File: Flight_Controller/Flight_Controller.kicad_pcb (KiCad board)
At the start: 4 copper layers, 123 parts, among them IC1 ICM-20689, J1 USB_C_Receptacle_USB2.0_16P, J2 SM08B-SRSS-TB, J3 SM04B-SRSS-TB, J4 SM06B-SRSS-TBLFSN, J5 SM03B-SRSS-TB, Q1 AO3400A, SW1 SW_Push, U1 NO, U11 ESD224DQA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

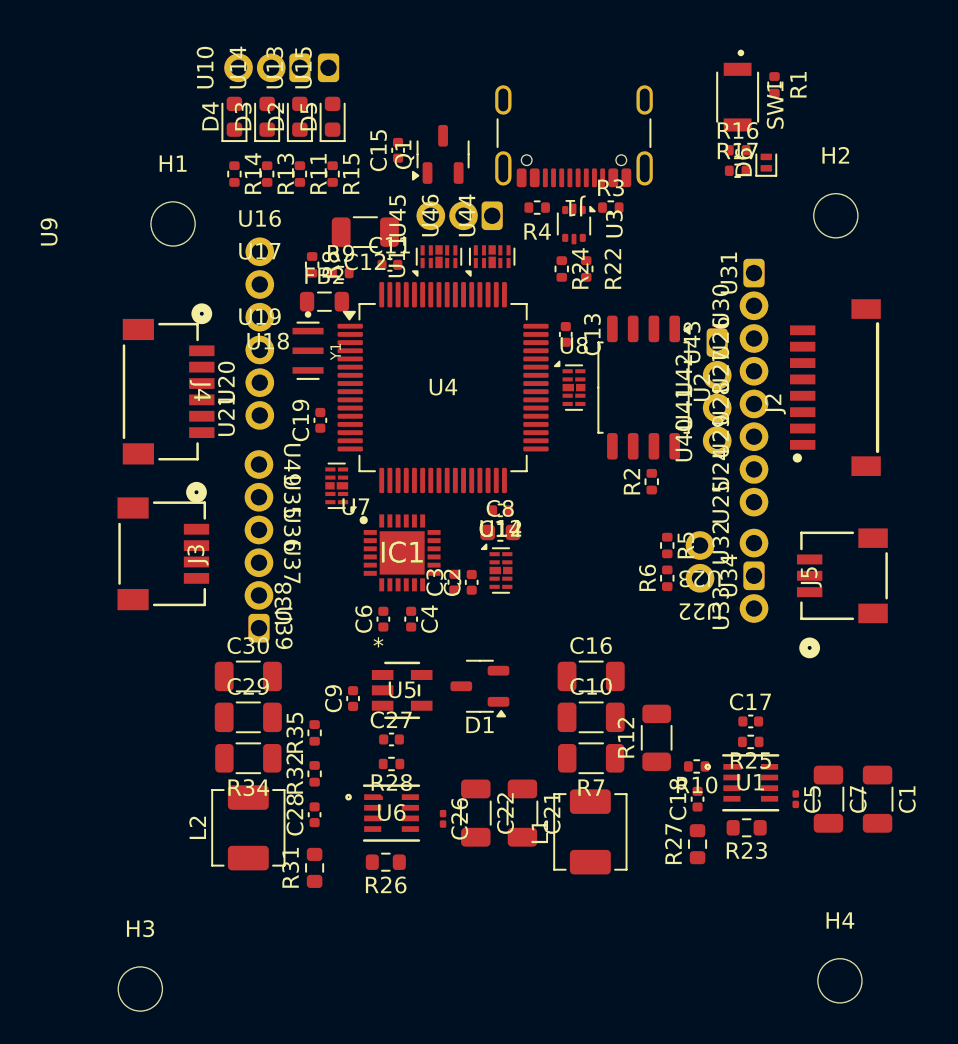
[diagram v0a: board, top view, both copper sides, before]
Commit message: Modificacion emplazamiento 2
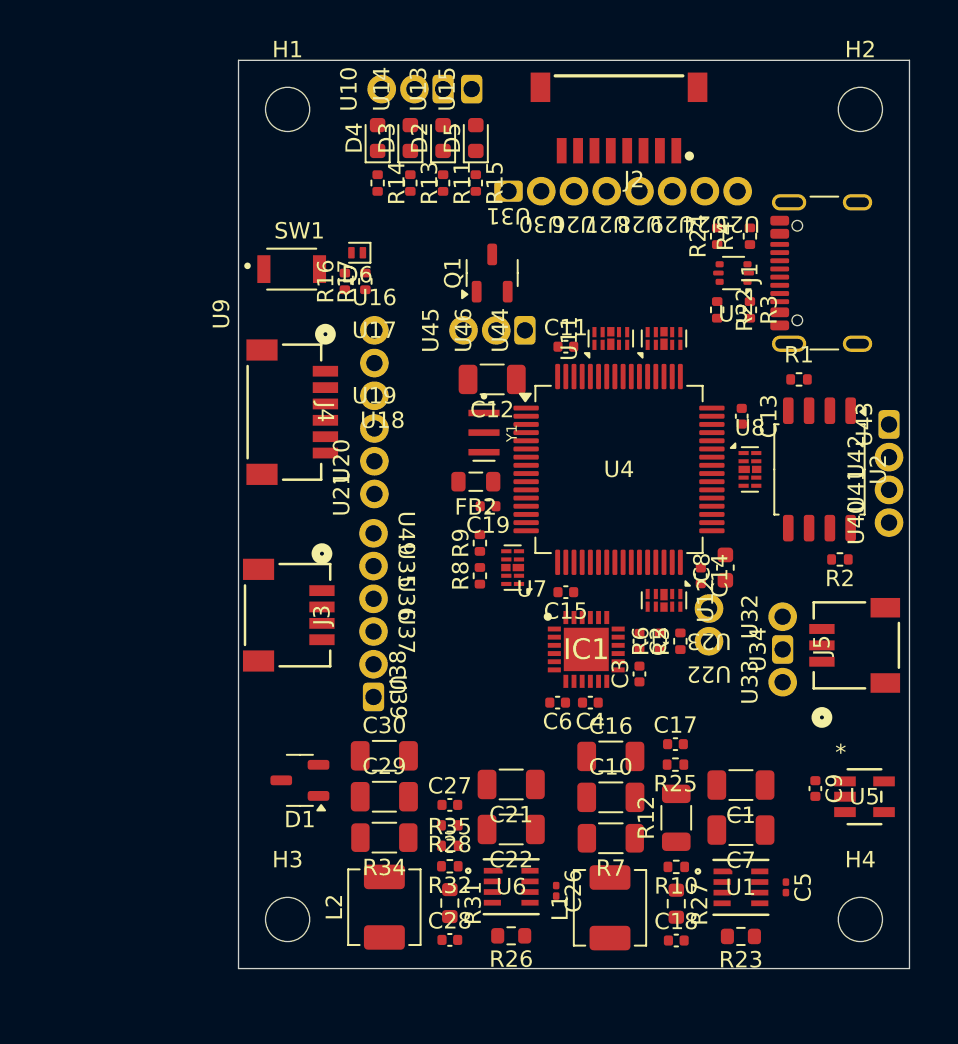
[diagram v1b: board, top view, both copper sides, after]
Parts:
- moved SW1 29.2 mm to (173.8, 79.3), turned to 0 degrees
- moved U5 29.0 mm to (208.8, 111.5)
- moved C15 28.9 mm to (190.5, 99.0), turned to 180 degrees
- moved C9 28.8 mm to (205.8, 111.0), turned to -90 degrees
- moved D6 25.6 mm to (177.8, 78.3), turned to 180 degrees
- moved R16 25.3 mm to (177.0, 80.0), turned to 90 degrees
- moved J2 25.0 mm to (193.8, 67.2), turned to 180 degrees
- moved R17 23.7 mm to (178.2, 80.0), turned to 90 degrees
- moved R8 21.6 mm to (185.2, 98.0), turned to 90 degrees
- moved U25 19.0 mm to (201.0, 74.5), turned to 180 degrees
- moved J1 18.8 mm to (207.2, 79.5), turned to 90 degrees
- moved R9 18.6 mm to (185.2, 96.0), turned to 90 degrees
- moved R1 18.1 mm to (204.8, 86.0), turned to 0 degrees
- moved U24 17.3 mm to (199.0, 74.5), turned to 180 degrees
- moved U29 15.8 mm to (197.0, 74.5), turned to 180 degrees
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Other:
- board outline added: 41 x 55.5 mm
